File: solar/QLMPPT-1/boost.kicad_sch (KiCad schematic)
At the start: 9 parts

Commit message: Continuing QLMPPT-1
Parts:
- removed D1, D2: MIC 20A10, symbol Device:D
- removed FH1: 15A, symbol Device:Fuse_Small
- removed RS3: R025, symbol Device:R
- removed RS4: n.p., symbol Device:R
- added L1: Power choke, symbol Device:L
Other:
- note added: "U6: 300MP249Z J1: 4-pin programming/uart header U3: 78L05 R36, R38 C7, C13, C22, C19 R39, R40, R41 R16, R17, R18 R21, R22, R23 C12, C17 U4: EG2132 totem pole gate driver low-side output controls T1 (n.p.) and T2 gates C6: U4 bypass D2: bootstrap diode C14 R15, R14, R19 RNTC1"
- note removed: "U6: 300MP249Z J1: 4-pin programming/uart header U3: 78L05 R36, R38 C7, C13, C22, C19 R39, R40, R41 R16, R17, R18 R21, R22, R23 C12, C17"
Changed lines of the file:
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@@
 (kicad_sch (version 20211123) (generator eeschema)
   (paper "A4")
-  (text "U6: 300MP249Z\nJ1: 4-pin programming/uart header\nU3: 78L05\nR36, R38\nC7, C13, C22, C19\nR39, R40, R41\nR16, R17, R18\nR21, R22, R23\nC12, C17"
+  (text "U6: 300MP249Z\nJ1: 4-pin programming/uart header\nU3: 78L05\nR36, R38\nC7, C13, C22, C19\nR39, R40, R41\nR16, R17, R18\nR21, R22, R23\nC12, C17\n\nU4: EG2132 totem pole gate driver\n  low-side output controls T1 (n.p.) and T2 gates\nC6: U4 bypass\nD2: bootstrap diode\nC14\nR15, R14, R19\nRNTC1"
     (at 83.185 97.79 0)
     (effects (font (size 1.27 1.27)) (justify left bottom))
+  )
+  (hierarchical_label "IN-" (shape bidirectional) (at 70.485 46.355 180)
+    (effects (font (size 1.27 1.27)) (justify right))
+  )
+  (hierarchical_label "IN+" (shape bidirectional) (at 70.485 40.005 180)
+    (effects (font (size 1.27 1.27)) (justify right))
+  )
+  (hierarchical_label "OUT+" (shape bidirectional) (at 70.485 52.07 180)
+    (effects (font (size 1.27 1.27)) (justify right))
+  )
+  (hierarchical_label "OUT-" (shape bidirectional) (at 70.485 58.42 180)
+    (effects (font (size 1.27 1.27)) (justify right))
   )
   (symbol (lib_id "Device:C_Polarized") (at 184.15 80.645 0) (unit 1)
@@
     )
     (property "Datasheet" "~" (id 3) (at 184.15 80.645 0)
-      (effects (font (size 1.27 1.27)) hide)
-    )
-    (pin "1")
-    (pin "2")
-  )
-  (symbol (lib_id "Device:R") (at 153.67 96.52 90) (unit 1)
-    (in_bom yes) (on_board yes) (fields_autoplaced)
-    (property "Reference" "RS3" (id 0) (at 153.67 91.8042 90))
-    (property "Value" "R025" (id 1) (at 153.67 94.3411 90))
-    (property "Footprint" "" (id 2) (at 153.67 98.298 90)
-      (effects (font (size 1.27 1.27)) hide)
-    )
-    (property "Datasheet" "~" (id 3) (at 153.67 96.52 0)
-      (effects (font (size 1.27 1.27)) hide)
-    )
-    (pin "1")
-    (pin "2")
-  )
-  (symbol (lib_id "Device:D") (at 140.97 59.055 0) (unit 1)
-    (in_bom yes) (on_board yes) (fields_autoplaced)
-    (property "Reference" "D1" (id 0) (at 140.97 54.0852 0))
-    (property "Value" "MIC 20A10" (id 1) (at 140.97 56.6221 0))
-    (property "Footprint" "" (id 2) (at 140.97 59.055 0)
-      (effects (font (size 1.27 1.27)) hide)
-    )
-    (property "Datasheet" "~" (id 3) (at 140.97 59.055 0)
       (effects (font (size 1.27 1.27)) hide)
     )
@@
     (pin "2")
   )
-  (symbol (lib_id "Device:R") (at 153.67 87.63 90) (unit 1)
-    (in_bom yes) (on_board yes)
-    (property "Reference" "RS4" (id 0) (at 153.67 82.9142 90))
-    (property "Value" "n.p." (id 1) (at 153.67 85.4511 90))
-    (property "Footprint" "" (id 2) (at 153.67 89.408 90)
-      (effects (font (size 1.27 1.27)) hide)
-    )
-    (property "Datasheet" "~" (id 3) (at 153.67 87.63 0)
-      (effects (font (size 1.27 1.27)) hide)
-    )
-    (pin "1")
-    (pin "2")
-  )
   (symbol (lib_id "Device:C_Polarized") (at 182.88 121.285 0) (unit 1)
     (in_bom yes) (on_board yes) (fields_autoplaced)
@@
     (pin "2")
   )
-  (symbol (lib_id "Device:D") (at 140.97 73.66 0) (unit 1)
+  (symbol (lib_id "Device:L") (at 143.51 93.98 0) (unit 1)
     (in_bom yes) (on_board yes) (fields_autoplaced)
-    (property "Reference" "D2" (id 0) (at 140.97 68.6902 0))
-    (property "Value" "MIC 20A10" (id 1) (at 140.97 71.2271 0))
-    (property "Footprint" "" (id 2) (at 140.97 73.66 0)
+    (property "Reference" "L1" (id 0) (at 144.78 93.1453 0)
+      (effects (font (size 1.27 1.27)) (justify left))
+    )
+    (property "Value" "Power choke" (id 1) (at 144.78 95.6822 0)
+      (effects (font (size 1.27 1.27)) (justify left))
+    )
+    (property "Footprint" "" (id 2) (at 143.51 93.98 0)
       (effects (font (size 1.27 1.27)) hide)
     )
-    (property "Datasheet" "~" (id 3) (at 140.97 73.66 0)
+    (property "Datasheet" "~" (id 3) (at 143.51 93.98 0)
       (effects (font (size 1.27 1.27)) hide)
     )
@@
     (pin "2")
   )
-  (symbol (lib_id "Device:Fuse_Small") (at 170.18 62.865 0) (unit 1)
-    (in_bom yes) (on_board yes) (fields_autoplaced)
-    (property "Reference" "FH1" (id 0) (at 170.18 58.7842 0))
-    (property "Value" "15A" (id 1) (at 170.18 61.3211 0))
-    (property "Footprint" "" (id 2) (at 170.18 62.865 0)
-      (effects (font (size 1.27 1.27)) hide)
-    )
-    (property "Datasheet" "~" (id 3) (at 170.18 62.865 0)
-      (effects (font (size 1.27 1.27)) hide)
-    )
-    (pin "1")
-    (pin "2")
-  )
   (sheet_instances
     (path "/" (page "1"))
@@
       (reference "C24") (unit 1) (value "100V,220uF") (footprint "")
     )
-    (path "/4cf63eea-9a02-4093-8de1-60abb2e1abd0"
-      (reference "D1") (unit 1) (value "MIC 20A10") (footprint "")
-    )
-    (path "/bc222fec-af97-4229-a75c-206d1f5d9026"
-      (reference "D2") (unit 1) (value "MIC 20A10") (footprint "")
-    )
-    (path "/e9f02310-f174-4e85-8da5-e0d6eb35e13a"
-      (reference "FH1") (unit 1) (value "15A") (footprint "")
-    )
-    (path "/22823d8b-86c7-4683-a40f-2893dd3480ee"
-      (reference "RS3") (unit 1) (value "R025") (footprint "")
-    )
-    (path "/9af9e1a5-ff93-4f67-a681-f0a780d2ee4f"
-      (reference "RS4") (unit 1) (value "n.p.") (footprint "")
+    (path "/a6520adb-7357-4ce3-b912-ecfc735d2ccf"
+      (reference "L1") (unit 1) (value "Power choke") (footprint "")
     )
   )

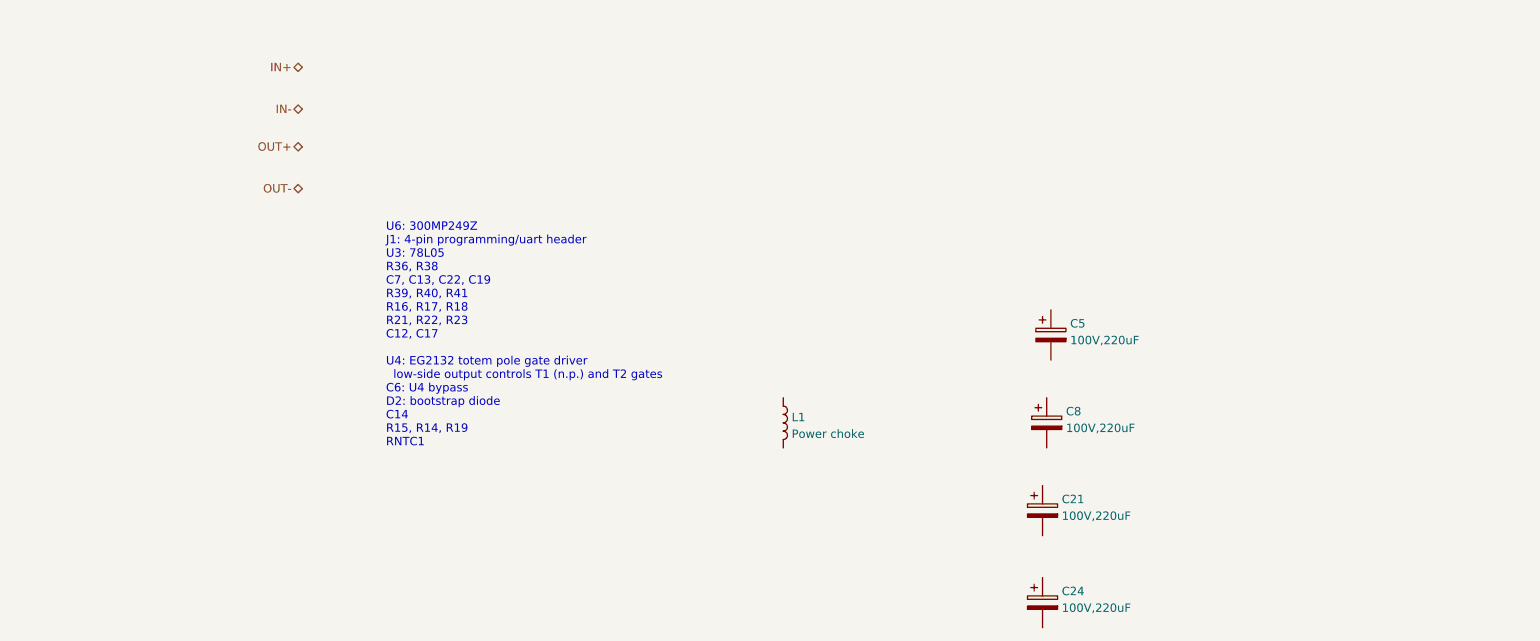
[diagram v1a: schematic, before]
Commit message: Sketching boost converter
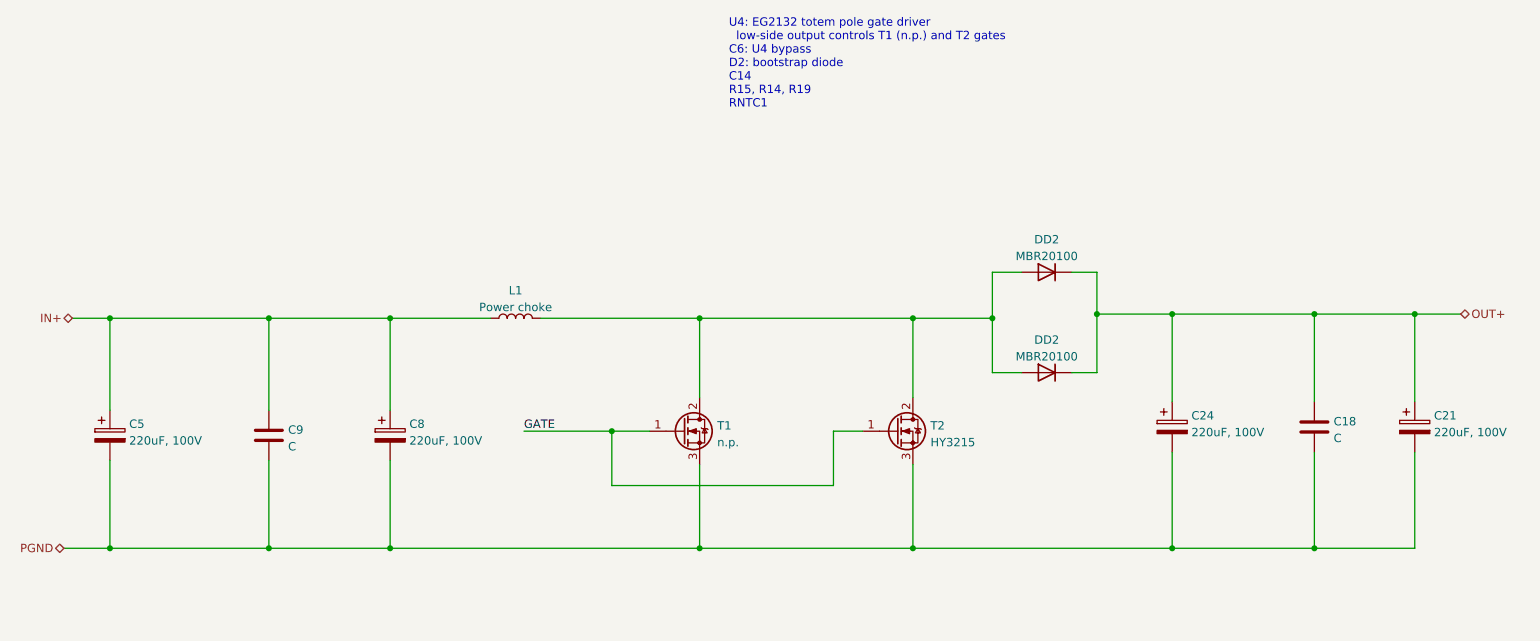
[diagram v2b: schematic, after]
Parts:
- added C18, C9: C, symbol Device:C
- added DD2 (x2): MBR20100, symbol Device:D
- added T1: n.p., symbol Device:Q_NMOS_GDS
- added T2: HY3215, symbol Device:Q_NMOS_GDS
- C21, C24, C5, C8: value 100V,220uF -> 220uF, 100V
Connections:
- net IN+: now also C5.1, C8.1, L1.1, C9.1
- net OUT+: now also C21.1, C24.1, C18.1, DD2.1 (K), DD2.1 (K)
- net PGND: now reaches C5.2
- net PGND: now also C21.2, C24.2, C8.2, C18.2, C9.2, T1.3 (S), T2.3 (S)
- net at L1.2: now also DD2.2 (A), DD2.2 (A), T1.2 (D), T2.2 (D)
- new net GATE: T1.1 (G), T2.1 (G)
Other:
- note added: "U4: EG2132 totem pole gate driver low-side output controls T1 (n.p.) and T2 gates C6: U4 bypass D2: bootstrap diode C14 R15, R14, R19 RNTC1"
- note removed: "U6: 300MP249Z J1: 4-pin programming/uart header U3: 78L05 R36, R38 C7, C13, C22, C19 R39, R40, R41 R16, R17, R18 R21, R22, R23 C12, C17 U4: EG2132 totem pole gate driver low-side output controls T1 (n.p.) and T2 gates C6: U4 bypass D2: bootstrap diode C14 R15, R14, R19 RNTC1"
- moved on the sheet: C21, C24, C5, C8, L1

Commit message: Continuing QLMPPT-1
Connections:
- net GATE renamed GATES_LOWSIDE
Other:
- note added: "Warum haben sie denn hier Dioden genommen? Der Treiber erzeugt High- und Low-Side-Gate-Pegel. Da könnte man sich einiges an Wärmeverlusten sparen, wenn man nicht den ganzen Strom über die Dioden pressen würde."
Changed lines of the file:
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@@
     (stroke (width 0) (type default) (color 0 0 0 0))
   )
-  (wire (pts (xy 104.14 95.25) (xy 117.475 95.25))
+  (wire (pts (xy 100.965 95.25) (xy 117.475 95.25))
     (stroke (width 0) (type default) (color 0 0 0 0))
   )
@@
   (wire (pts (xy 34.29 113.03) (xy 41.275 113.03))
     (stroke (width 0) (type default) (color 0 0 0 0))
+  )
+  (text "Warum haben sie denn hier Dioden genommen?\nDer Treiber erzeugt High- und Low-Side-Gate-Pegel.\nDa könnte man sich einiges an Wärmeverlusten sparen,\nwenn man nicht den ganzen Strom über die Dioden pressen würde.\n"
+    (at 174.625 64.135 0)
+    (effects (font (size 1.27 1.27)) (justify left bottom))
   )
   (text "U4: EG2132 totem pole gate driver\n  low-side output controls T1 (n.p.) and T2 gates\nC6: U4 bypass\nD2: bootstrap diode\nC14\nR15, R14, R19\nRNTC1"
@@
     (effects (font (size 1.27 1.27)) (justify left bottom))
   )
-  (label "GATE" (at 104.14 95.25 0)
+  (label "GATES_LOWSIDE" (at 100.965 95.25 0)
     (effects (font (size 1.27 1.27)) (justify left bottom))
   )
@@
       (reference "C8") (unit 1) (value "100V,220uF") (footprint "")
     )
+    (path "/9e4dd27c-8e1b-4c51-ad64-2ada413c46a3"
+      (reference "C9") (unit 1) (value "C") (footprint "")
+    )
+    (path "/219b5efc-4843-4ea5-8e07-64985af50eae"
+      (reference "C18") (unit 1) (value "C") (footprint "")
+    )
     (path "/4f02867a-7c2f-4c41-b9bd-b4958cb5319c"
       (reference "C21") (unit 1) (value "100V,220uF") (footprint "")
@@
       (reference "C24") (unit 1) (value "100V,220uF") (footprint "")
     )
+    (path "/1eee681b-dc8a-49ce-94eb-3c0bdb231f5c"
+      (reference "DD2") (unit 1) (value "MBR20100") (footprint "")
+    )
+    (path "/9c97b038-096e-4af4-8d5b-ef800d569788"
+      (reference "DD2") (unit 1) (value "MBR20100") (footprint "")
+    )
     (path "/a6520adb-7357-4ce3-b912-ecfc735d2ccf"
       (reference "L1") (unit 1) (value "Power choke") (footprint "")
     )
-  )
+    (path "/4835ca46-a6b1-4095-8301-cbbdf1f05417"
+      (reference "T1") (unit 1) (value "n.p.") (footprint "")
+    )
+    (path "/2ef1900b-23f8-4d9d-9ce6-61794b81b68e"
+      (reference "T2") (unit 1) (value "HY3215") (footprint "")
+    )
+  )
